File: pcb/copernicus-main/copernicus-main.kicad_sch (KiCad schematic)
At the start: 3 parts, among them J1 Screw_Terminal_01x02, SW1 PWR_BTN, SW2 ESTOP

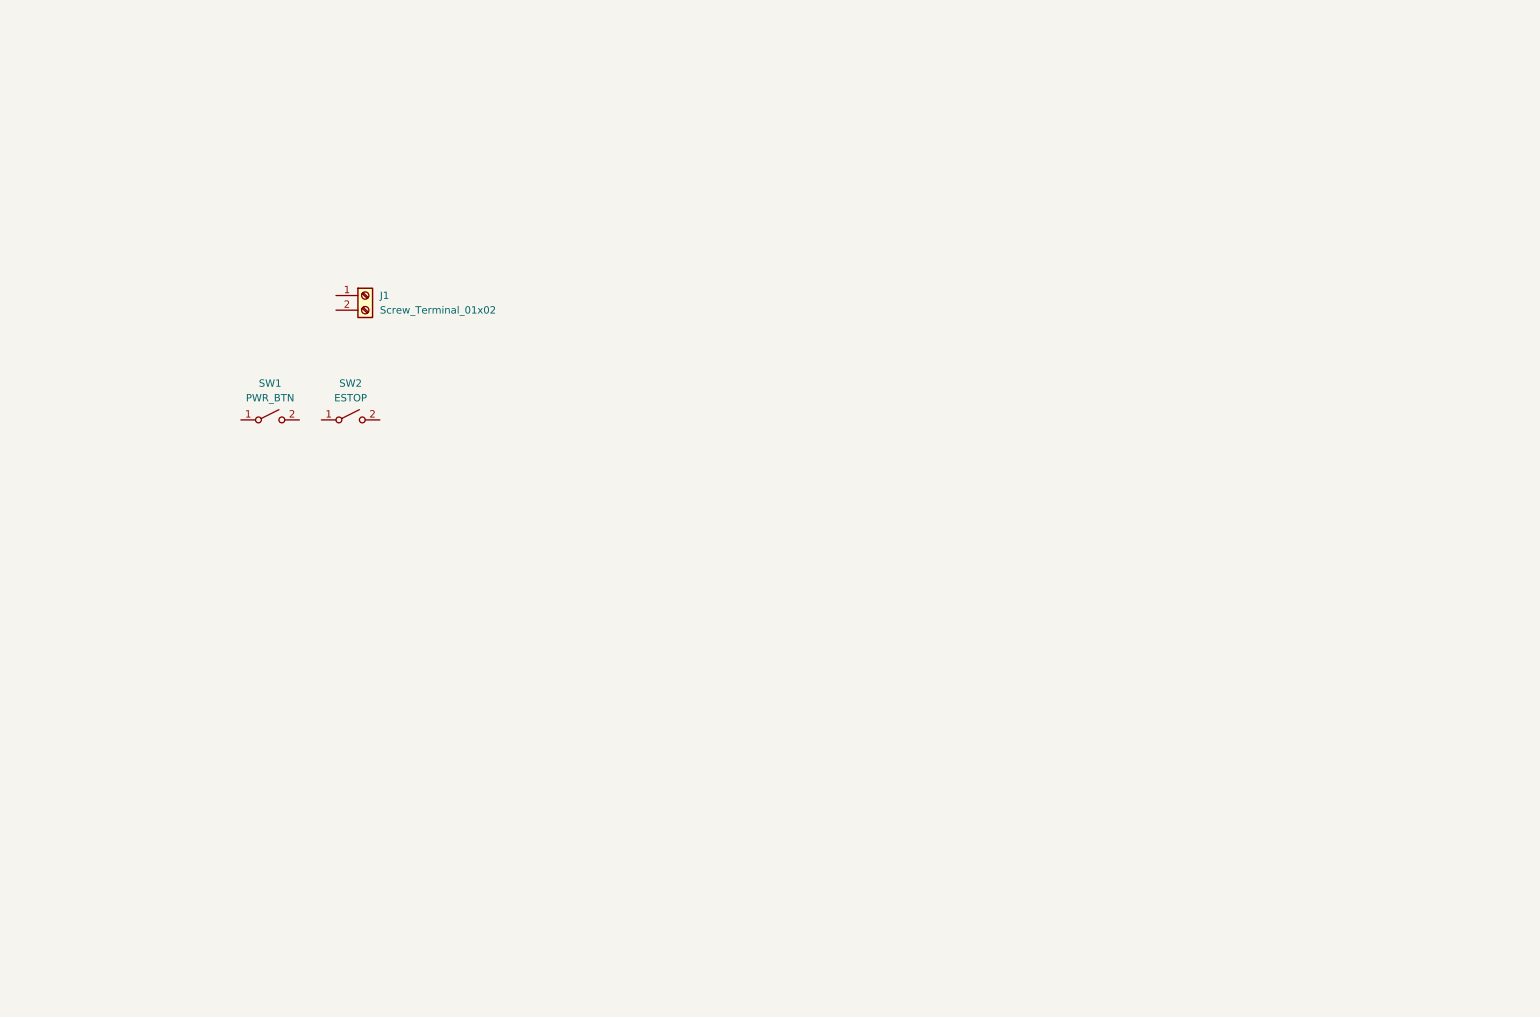
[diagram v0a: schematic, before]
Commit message: docs(pcb): crytal design & mcu selection
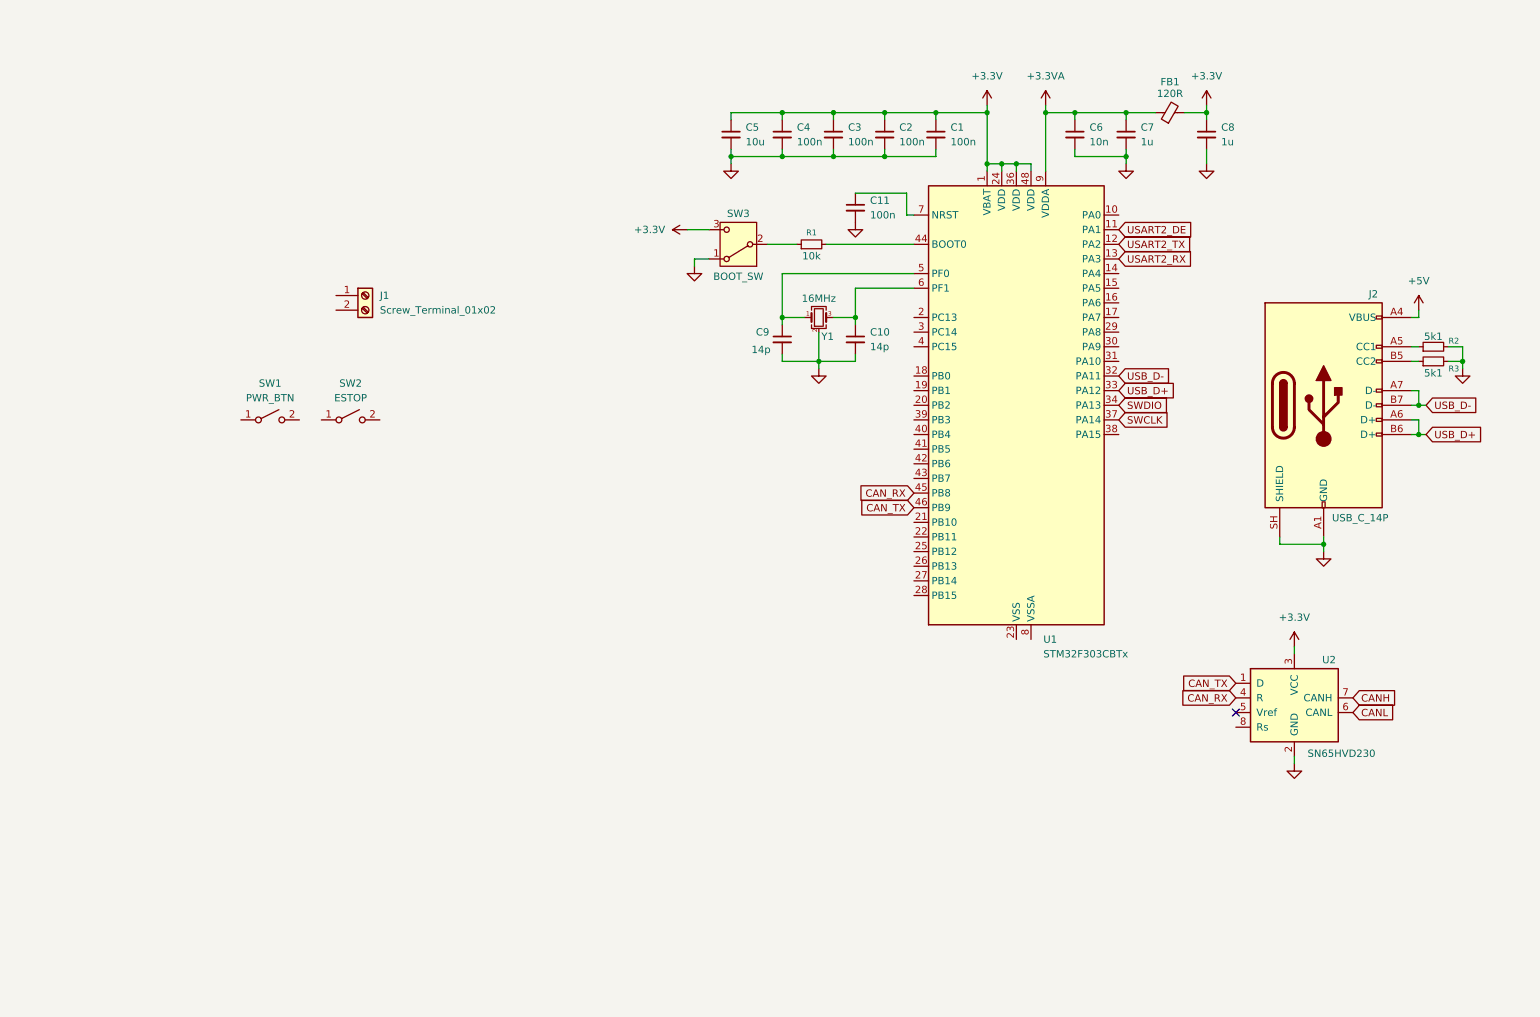
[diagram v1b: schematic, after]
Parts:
- added C1, C11, C2, C3, C4: 100n, symbol Device:C_Small
- added C10, C9: 14p, symbol Device:C_Small
- added C5: 10u, symbol Device:C_Small
- added C6: 10n, symbol Device:C_Small
- added C7, C8: 1u, symbol Device:C_Small
- added FB1: 120R, symbol Device:FerriteBead_Small
- added J2: USB_C_14P, symbol Connector:USB_C_Receptacle_USB2.0_14P
- added R1: 10k, symbol Device:R_Small
- added R2, R3: 5k1, symbol Device:R_Small
- added SW3: BOOT_SW, symbol Switch:SW_SPDT
- added U1: STM32F303CBTx, Package_QFP:LQFP-48_7x7mm_P0.5mm, symbol MCU_ST_STM32F3:STM32F303CBTx
- added U2: SN65HVD230, Package_SO:SOIC-8_3.9x4.9mm_P1.27mm, symbol Interface_CAN_LIN:SN65HVD230
- added Y1: 16MHz, symbol Device:Crystal_GND24_Small
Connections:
- new net: R1.1, SW3.2 (B)
- new net: R1.2, U1.44 (BOOT0)
- new net: J2.B5 (CC2), R3.1
- new net: U1.23 (VSS), U1.35 (VSS), U1.47 (VSS)
- new net: C9.1, U1.5 (PF0), Y1.1
- new net: C10.1, U1.6 (PF1), Y1.3
- new net: C11.1, U1.7 (NRST)
- new net: J2.A5 (CC1), R2.1
- new net +3.3V: C1.1, C2.1, C3.1, C4.1, C5.1, C8.1, FB1.2, SW3.3 (C), U1.1 (VBAT), U1.24 (VDD), U1.36 (VDD), U1.48 (VDD), U2.3 (VCC)
- new net +3.3VA: C6.1, C7.1, FB1.1, U1.9 (VDDA)
- new net +5V: J2.A4 (VBUS), J2.A9 (VBUS), J2.B4 (VBUS), J2.B9 (VBUS)
- new net CANH: U2.7 (CANH)
- new net CANL: U2.6 (CANL)
- new net CAN_RX: U1.45 (PB8), U2.4 (R)
- new net CAN_TX: U1.46 (PB9), U2.1 (D)
- new net GND: C1.2, C10.2, C11.2, C2.2, C3.2, C4.2, C5.2, C6.2, C7.2, C8.2, C9.2, J2.A1 (GND), J2.A12 (GND), J2.B1 (GND), J2.B12 (GND), J2.SH (SHIELD), R2.2, R3.2, SW3.1 (A), U2.2 (GND), Y1.2 (G), Y1.4 (G)
- new net SWCLK: U1.37 (PA14)
- new net SWDIO: U1.34 (PA13)
- new net USART2_DE: U1.11 (PA1)
- new net USART2_RX: U1.13 (PA3)
- new net USART2_TX: U1.12 (PA2)
- new net USB_D+: J2.A6 (D+), J2.B6 (D+), U1.33 (PA12)
- new net USB_D-: J2.A7 (D-), J2.B7 (D-), U1.32 (PA11)
- no-connect marks 0 -> 1

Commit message: commit
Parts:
- added C12: 10n, symbol Device:C_Small
- added C13: 100n, symbol Device:C_Small
- added R4, R5: 60, symbol Device:R_Small
- added SW4: SW_DPST, symbol Switch:SW_DPST
- added U3: USBLC6-2SC6, Package_TO_SOT_SMD:SOT-23-6, symbol Power_Protection:USBLC6-2SC6
- added U4: THVD1450D, Package_SO:SOIC-8_3.9x4.9mm_P1.27mm, symbol Interface_UART:THVD1450D
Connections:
- net +5V: now also C13.1, U3.5 (VBUS)
- net CANH: now also SW4.3
- net CANL: now also SW4.1
- net GND: now also U2.8 (Rs), C12.2, C13.2, U3.2 (GND)
- net USB_D+: now also U3.4 (I/O2); no longer J2.A6 (D+), J2.B6 (D+)
- net USB_D-: now also U3.6 (I/O1); no longer J2.A7 (D-), J2.B7 (D-)
- new net: C12.1, R4.1, R5.1
- new net: R4.2, SW4.4
- new net: R5.2, SW4.2
- new net: J2.A7 (D-), J2.B7 (D-), U3.1 (I/O1)
- new net: J2.A6 (D+), J2.B6 (D+), U3.3 (I/O2)
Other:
- moved on the sheet: J2, R2, R3, U2

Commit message: commmit
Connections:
- net GND: now also U4.5 (GND)
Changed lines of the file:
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@@
+	(wire
+		(pts
+			(xy 143.51 149.86) (xy 143.51 151.13)
+		)
+		(stroke
+			(width 0)
+			(type default)
+		)
+	)
 	(wire
 		(pts
@@
 		(in_pos_files yes)
 		(dnp no)
-		(fields_autoplaced yes)
 		(property "Reference" "U4"
-			(at 145.6533 116.84 0)
+			(at 148.082 120.396 0)
 			(show_name no)
 			(do_not_autoplace no)
@@
 		)
 		(property "Value" "THVD1450D"
-			(at 145.6533 119.38 0)
+			(at 145.034 149.098 0)
 			(show_name no)
 			(do_not_autoplace no)
@@
 					(unit 1)
 				)
+			)
+		)
+	)
+	(symbol
+		(lib_id "power:GND")
+		(at 143.51 151.13 0)
+		(unit 1)
+		(body_style 1)
+		(exclude_from_sim no)
+		(in_bom yes)
+		(on_board yes)
+		(in_pos_files yes)
+		(dnp no)
+		(fields_autoplaced yes)
+		(property "Reference" "#PWR019"
+			(at 143.51 157.48 0)
+			(hide yes)
+			(show_name no)
+			(do_not_autoplace no)
+			(effects
+				(font
+					(size 1.27 1.27)
+				)
+			)
+		)
+		(property "Value" "GND"
+			(at 143.51 156.21 0)
+			(hide yes)
+			(show_name no)
+			(do_not_autoplace no)
+			(effects
+				(font
+					(size 1.27 1.27)
+				)
+			)
+		)
+		(property "Footprint" ""
+			(at 143.51 151.13 0)
+			(hide yes)
+			(show_name no)
+			(do_not_autoplace no)
+			(effects
+				(font
+					(size 1.27 1.27)
+				)
+			)
+		)
+		(property "Datasheet" ""
+			(at 143.51 151.13 0)
+			(hide yes)
+			(show_name no)
+			(do_not_autoplace no)
+			(effects
+				(font
+					(size 1.27 1.27)
+				)
+			)
+		)
+		(property "Description" "Power symbol creates a global label with name \"GND\" , ground"
+			(at 143.51 151.13 0)
+			(hide yes)
+			(show_name no)
+			(do_not_autoplace no)
+			(effects
+				(font
+					(size 1.27 1.27)
+				)
+			)
+		)
+		(pin "1"
+		)
+		(instances
+			(project "copernicus-main"
+				(path "/a9180fc8-dc83-4e73-a866-5c9cdd0f4d7b"
+					(reference "#PWR019")
+					(unit 1)
+				)

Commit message: commit
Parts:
- added U5: THVD1400D, Package_SO:SOIC-8_3.9x4.9mm_P1.27mm, symbol Interface_UART:THVD1400D
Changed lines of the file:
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@@
+	)
+	(symbol
+		(lib_id "Interface_UART:THVD1400D")
+		(at 120.65 101.6 0)
+		(unit 1)
+		(body_style 1)
+		(exclude_from_sim no)
+		(in_bom yes)
+		(on_board yes)
+		(in_pos_files yes)
+		(dnp no)
+		(fields_autoplaced yes)
+		(property "Reference" "U5"
+			(at 122.7933 83.82 0)
+			(show_name no)
+			(do_not_autoplace no)
+			(effects
+				(font
+					(size 1.27 1.27)
+				)
+				(justify left)
+			)
+		)
+		(property "Value" "THVD1400D"
+			(at 122.7933 86.36 0)
+			(show_name no)
+			(do_not_autoplace no)
+			(effects
+				(font
+					(size 1.27 1.27)
+				)
+				(justify left)
+			)
+		)
+		(property "Footprint" "Package_SO:SOIC-8_3.9x4.9mm_P1.27mm"
+			(at 120.65 119.38 0)
+			(hide yes)
+			(show_name no)
+			(do_not_autoplace no)
+			(effects
+				(font
+					(size 1.27 1.27)
+				)
+			)
+		)
+		(property "Datasheet" "https://www.ti.com/lit/ds/symlink/thvd1420.pdf"
+			(at 120.65 100.33 0)
+			(hide yes)
+			(show_name no)
+			(do_not_autoplace no)
+			(effects
+				(font
+					(size 1.27 1.27)
+				)
+			)
+		)
+		(property "Description" "Half duplex RS-485/RS-422, 500 Kbps, 3V - 5.5V supply, ±12kV electro-static discharge (ESD) protection, with receiver/driver enable, 32 receiver drive capacity, SOIC-8"
+			(at 120.65 101.6 0)
+			(hide yes)
+			(show_name no)
+			(do_not_autoplace no)
+			(effects
+				(font
+					(size 1.27 1.27)
+				)
+			)
+		)
+		(pin "1"
+		)
+		(pin "2"
+		)
+		(pin "3"
+		)
+		(pin "4"
+		)
+		(pin "5"
+		)
+		(pin "6"
+		)
+		(pin "7"
+		)
+		(pin "8"
+		)
+		(instances
+			(project "copernicus-main"
+				(path "/a9180fc8-dc83-4e73-a866-5c9cdd0f4d7b"
+					(reference "U5")
+					(unit 1)
+				)
+			)
+		)
 	)
 	(symbol

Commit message: commit
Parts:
- removed U4: THVD1450D, Package_SO:SOIC-8_3.9x4.9mm_P1.27mm, symbol Interface_UART:THVD1450D
- added C14: 100n, symbol Device:C_Small
- added D1: SM712, Package_TO_SOT_SMD:SOT-23, symbol Diode:SM712_SOT23
- added R6, R7: 10k, symbol Device:R_Small
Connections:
- net +3.3V: now also U5.8 (VCC), C14.1, R6.1
- net GND: now also U5.5 (GND), C14.2, D1.3 (common), R7.2
- net USART2_DE: now also U5.2 (~{RE}), U5.3 (DE), R7.1
- net USART2_RX: now also U5.1 (RO), R6.2
- net USART2_TX: now also U5.4 (DI)
- net RS485+: now reaches U5.6 (A)
- net RS485+: now also D1.1 (A1)
- net RS485-: now reaches U5.7 (B)
- net RS485-: now also D1.2 (A2)
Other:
- moved on the sheet: U5

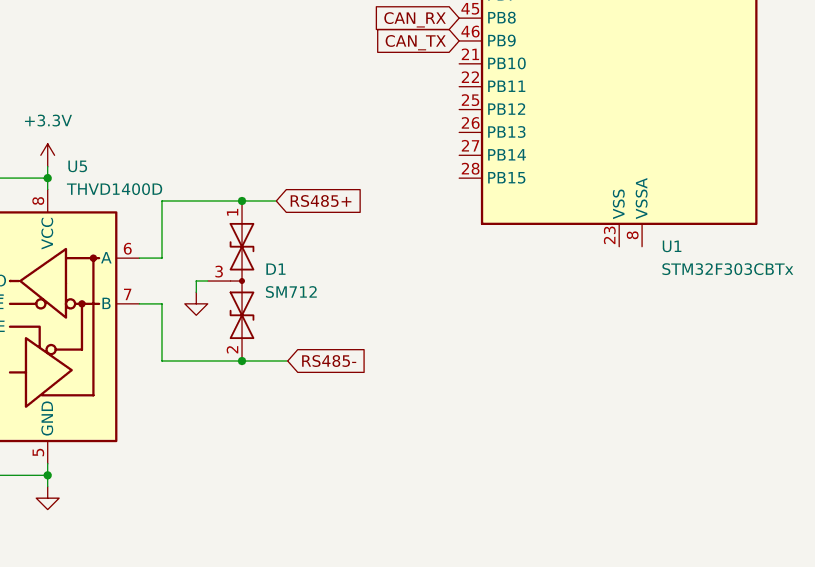
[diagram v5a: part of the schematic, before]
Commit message: config(mcu): changed stm32 mcu cubemx config
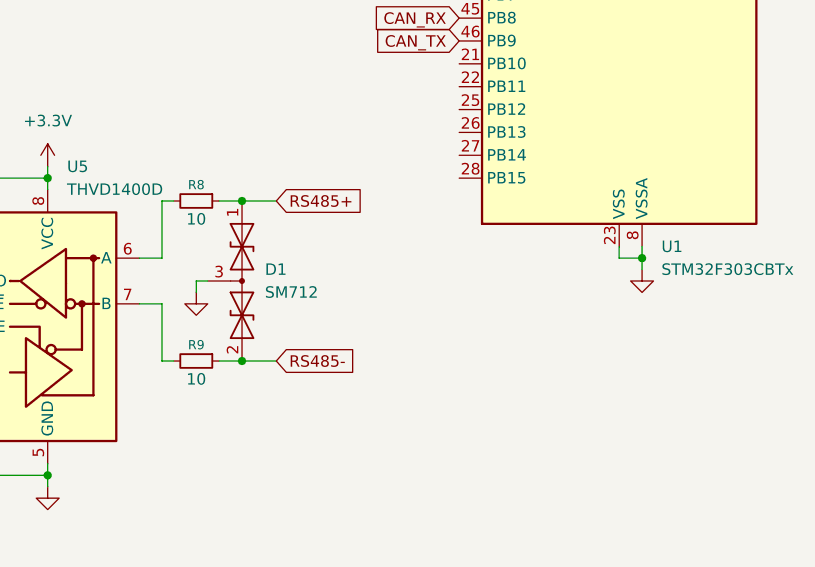
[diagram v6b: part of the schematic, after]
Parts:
- added R8, R9: 10, symbol Device:R_Small
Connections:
- net GND: now also U1.23 (VSS), U1.35 (VSS), U1.47 (VSS), U1.8 (VSSA)
- net RS485+: now also R8.1; no longer U5.6 (A)
- net RS485-: now also R9.1; no longer U5.7 (B)
- new net: R8.2, U5.6 (A)
- new net: R9.2, U5.7 (B)
